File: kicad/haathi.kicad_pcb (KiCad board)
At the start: 4 copper layers, 1 part

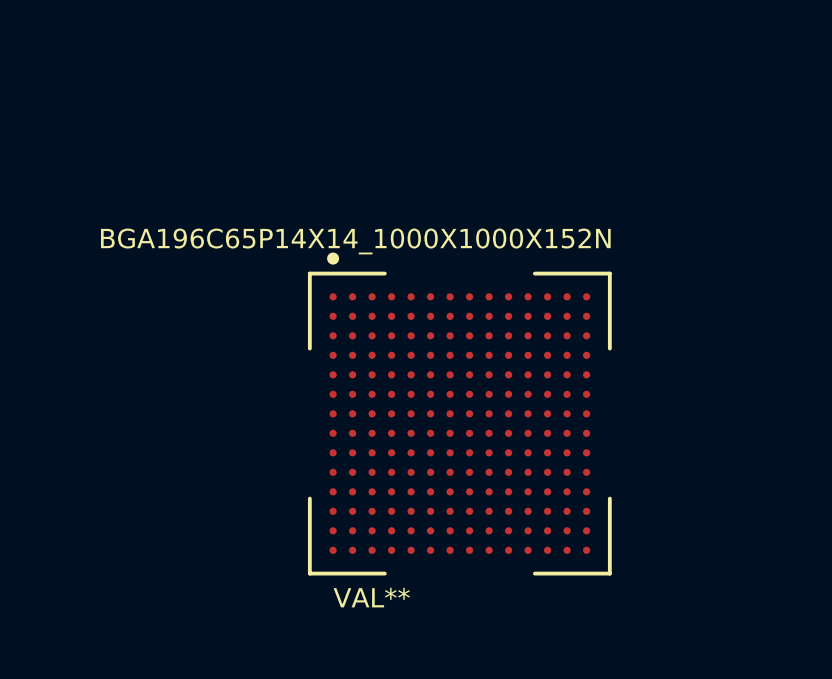
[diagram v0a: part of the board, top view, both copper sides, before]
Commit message: added BGA routing guides
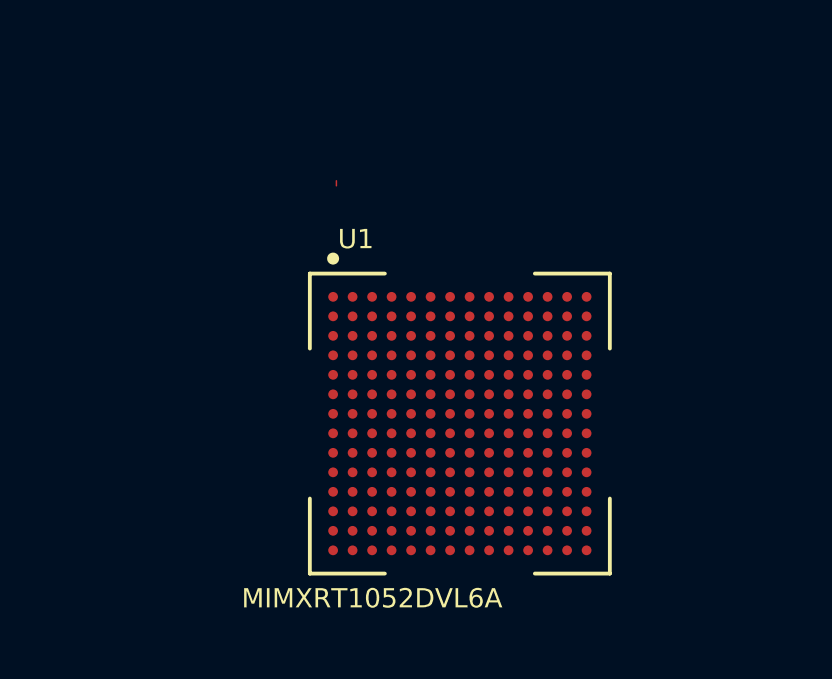
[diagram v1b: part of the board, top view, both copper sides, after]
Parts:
- removed BGA196C65P14X14_1000X1000X152N: VAL**, footprint_lib:BGA196C65P14X14_1000X1000X152N
- added U1: MIMXRT1052DVL6A, footprint_lib:BGA196C65P14X14_1000X1000X152N_v2, F.Cu at (100.0, 100.0)
